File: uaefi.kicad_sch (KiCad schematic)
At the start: 68 parts, among them J1 Conn_02x02_Odd_Even, J1 USB_B_Mini, J1 USB_C, J10 5569-16A2, J11 Conn_02x02_Odd_Even, J12 Conn_02x02_Odd_Even, J13 Conn_02x02_Odd_Even, J14 Conn_02x02_Odd_Even, J15 Conn_02x02_Odd_Even, J16 Conn_02x02_Odd_Even, J17 Conn_01x06, J17 Conn_02x02_Odd_Even, J18 Conn_02x02_Odd_Even, J19 Conn_02x02_Odd_Even, J2 5569-20A2, J20 Conn_02x02_Odd_Even, J21 Conn_02x02_Odd_Even, J22 Conn_02x02_Odd_Even, J24 Conn_02x02_Odd_Even, J3 5569-06A2, J4 5569-08A2, J5 5569-18A2, J5 Conn_01x05_Male, M1 Module-power_12and5V-0.2, M3 Module-knock-0.2, M3 Module-vr-discrete-0.5, M4 Module-vr-max9924-0.1, M5 Module-wbo-0.5, M6 Module:mega-mcu100/0.3, M7 Module-can-0.1, P1 Pad, P2 Pad, P3 Pad, P4 Pad, P5 Pad, P6 Pad, P7 Pad, P8 Pad, U4 JDY-33

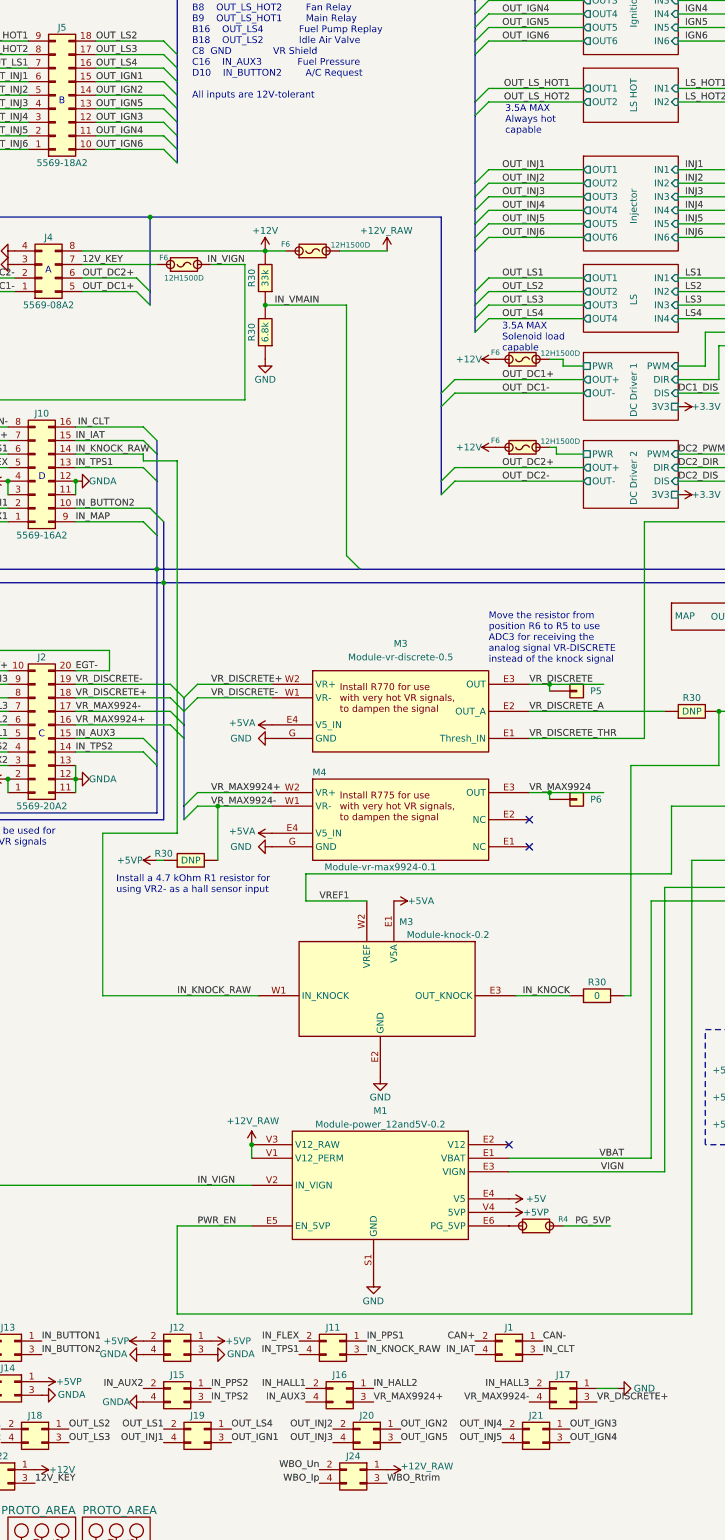
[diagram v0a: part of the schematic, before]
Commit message: tyring to make the pcb a two layer board
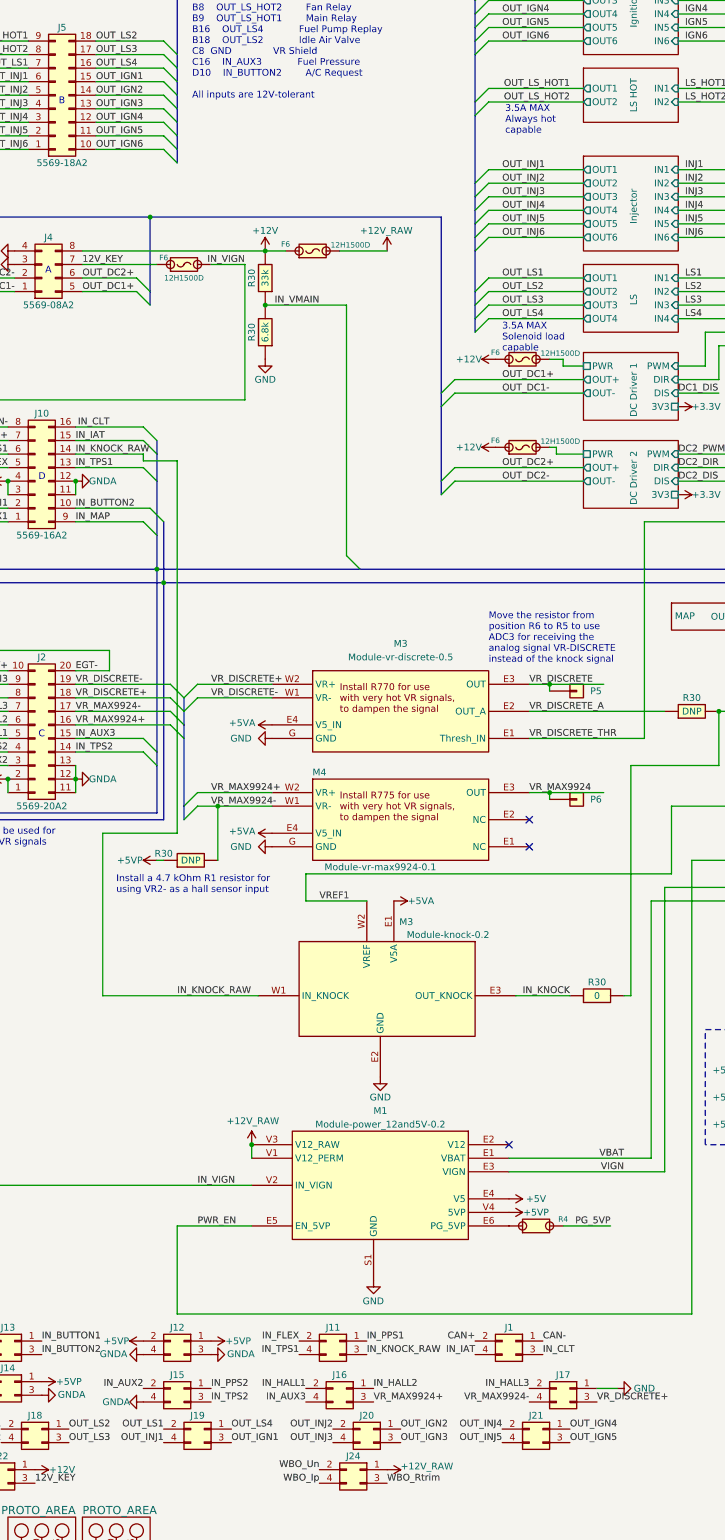
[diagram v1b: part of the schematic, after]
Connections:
- net OUT_IGN3: now also J20.3 (Pin_3), J5.13 (Pin_13); no longer J21.1 (Pin_1), J5.12 (Pin_12)
- net OUT_IGN4: now also J21.1 (Pin_1), J5.12 (Pin_12); no longer J21.3 (Pin_3), J5.11 (Pin_11)
- net OUT_IGN5: now also J21.3 (Pin_3), J5.11 (Pin_11); no longer J20.3 (Pin_3), J5.13 (Pin_13)
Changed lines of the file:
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@@
 	)
 	(label "OUT_IGN3"
-		(at 44.45 110.49 0)
+		(at 44.45 107.95 0)
 		(fields_autoplaced yes)
 		(effects
@@
 	)
 	(label "OUT_IGN5"
-		(at 101.6 358.14 0)
+		(at 133.35 358.14 0)
 		(fields_autoplaced yes)
 		(effects
@@
 	)
 	(label "OUT_IGN4"
-		(at 133.35 358.14 0)
+		(at 133.35 355.6 0)
 		(fields_autoplaced yes)
 		(effects
@@
 	)
 	(label "OUT_IGN5"
-		(at 44.45 107.95 0)
+		(at 44.45 113.03 0)
 		(fields_autoplaced yes)
 		(effects
@@
 	)
 	(label "OUT_IGN4"
-		(at 44.45 113.03 0)
+		(at 44.45 110.49 0)
 		(fields_autoplaced yes)
 		(effects
@@
 	)
 	(label "OUT_IGN3"
-		(at 133.35 355.6 0)
-		(fields_autoplaced yes)
-		(effects
+		(at 101.6 358.14 0)
+		(fields_autoplaced yes)
+		(effects
